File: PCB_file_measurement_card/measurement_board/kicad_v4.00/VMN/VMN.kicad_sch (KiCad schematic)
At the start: 43 parts, among them J1 A/B, J2 Screw_Terminal_VMN, J3 Alim DPH5005, J4 Raspberry_Pi_2_3, K1 AQY211EH, K2 AQY211EH, K3 AQY211EH, K4 AQY211EH, U1 INA128, U2 MCP23008-xP, U3 LM358, U4 INA282, U5 1085-Adress=0X49, U6 1085-Adress=0X48, U7 ISO1540

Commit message: Adds a first version of the PCB to be checked...
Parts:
- R6: footprint Resistor_THT:R_Axial_DIN0411_L9.9mm_D3.6mm_P15.24mm_Horizontal -> Resistor_THT:R_Axial_DIN0414_L11.9mm_D4.5mm_P20.32mm_Horizontal
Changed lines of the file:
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@@
       (effects (font (size 1.27 1.27)) (justify left))
     )
-    (property "Footprint" "Resistor_THT:R_Axial_DIN0411_L9.9mm_D3.6mm_P15.24mm_Horizontal" (id 2) (at 107.442 133.35 90)
+    (property "Footprint" "Resistor_THT:R_Axial_DIN0414_L11.9mm_D4.5mm_P20.32mm_Horizontal" (id 2) (at 107.442 133.35 90)
       (effects (font (size 1.27 1.27)) hide)
     )
@@
   (symbol (lib_id "Device:R") (at 86.36 80.01 0) (unit 1)
     (in_bom yes) (on_board yes)
-    (property "Reference" "R3" (id 0) (at 85.09 80.01 0)
-      (effects (font (size 0.75 0.75)) (justify left))
-    )
-    (property "Value" "1k" (id 1) (at 90.17 82.5499 0)
+    (property "Reference" "R3" (id 0) (at 83.82 78.74 90)
+      (effects (font (size 1.27 1.27)) (justify left))
+    )
+    (property "Value" "1k" (id 1) (at 86.36 81.28 90)
       (effects (font (size 1.27 1.27)) (justify left))
     )
@@
     )
     (path "/4aa539a9-6f3d-4fc3-b2d6-8348016bf7c3"
-      (reference "R6") (unit 1) (value "2") (footprint "Resistor_THT:R_Axial_DIN0411_L9.9mm_D3.6mm_P15.24mm_Horizontal")
+      (reference "R6") (unit 1) (value "2") (footprint "Resistor_THT:R_Axial_DIN0414_L11.9mm_D4.5mm_P20.32mm_Horizontal")
     )
     (path "/cd253d18-2c33-4027-8d8b-dc6d99e23181"

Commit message: update pcb board
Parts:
- added J6: Conn_02x03_Top_Bottom, symbol Connector_Generic:Conn_02x03_Top_Bottom
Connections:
- no-connect marks 56 -> 62
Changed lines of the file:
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@@
   (no_connect (at 153.67 72.39))
   (no_connect (at 153.67 77.47))
+  (no_connect (at 201.93 107.95))
+  (no_connect (at 201.93 110.49))
+  (no_connect (at 201.93 113.03))
+  (no_connect (at 189.23 113.03))
+  (no_connect (at 189.23 110.49))
+  (no_connect (at 189.23 107.95))
   (no_connect (at 252.73 35.56))
   (no_connect (at 255.27 35.56))
@@
     )
     (pin "1")
+  )
+  (symbol (lib_id "Connector_Generic:Conn_02x03_Top_Bottom") (at 194.31 110.49 0) (unit 1)
+    (in_bom yes) (on_board yes) (fields_autoplaced)
+    (property "Reference" "J6" (id 0) (at 195.58 101.6 0))
+    (property "Value" "Conn_02x03_Top_Bottom" (id 1) (at 195.58 104.14 0))
+    (property "Footprint" "" (id 2) (at 194.31 110.49 0)
+      (effects (font (size 1.27 1.27)) hide)
+    )
+    (property "Datasheet" "~" (id 3) (at 194.31 110.49 0)
+      (effects (font (size 1.27 1.27)) hide)
+    )
+    (pin "1")
+    (pin "2")
+    (pin "3")
+    (pin "4")
+    (pin "5")
+    (pin "6")
   )
   (symbol (lib_id "Device:R") (at 109.22 133.35 0) (unit 1)
@@
       (reference "J5") (unit 1) (value "Screw_Terminal_01x02") (footprint "TerminalBlock_Phoenix:TerminalBlock_Phoenix_MKDS-1,5-2-5.08_1x02_P5.08mm_Horizontal")
     )
+    (path "/49058ded-2ed2-473c-ba90-e52b2c428f78"
+      (reference "J6") (unit 1) (value "Conn_02x03_Top_Bottom") (footprint "Connector_IDC:IDC-Header_2x03_P2.54mm_Vertical")
+    )
     (path "/e76f0b41-8ed2-4982-8e0f-a0a6400944d9"

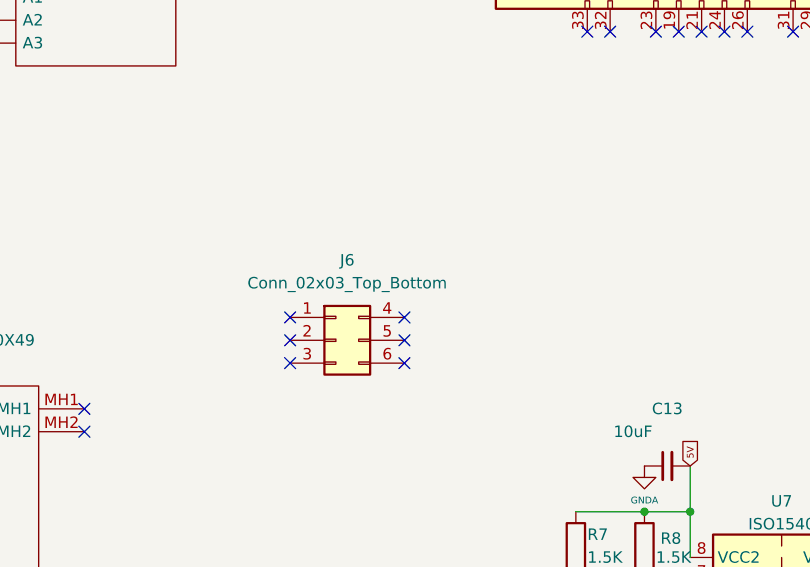
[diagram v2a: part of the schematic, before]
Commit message: update pcb board: +6 pin
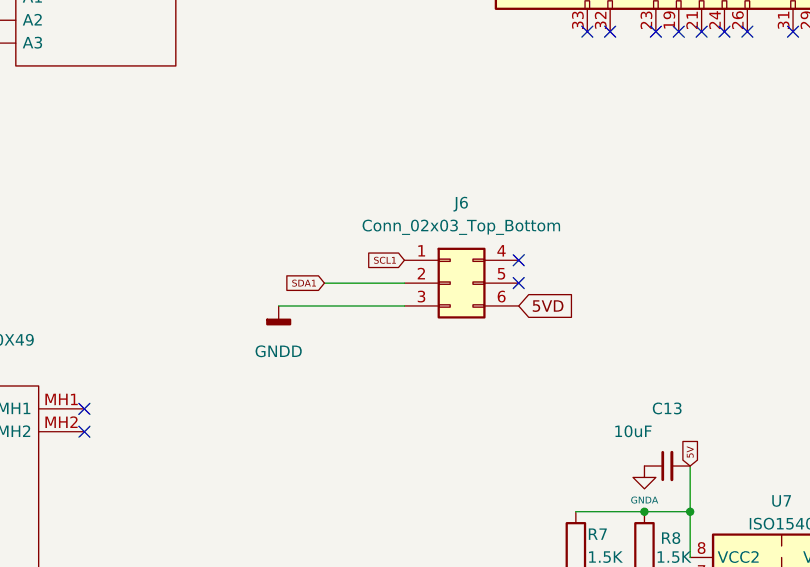
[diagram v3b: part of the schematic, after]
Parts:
- J6: footprint (none) -> Connector_IDC:IDC-Header_2x03_P2.54mm_Vertical
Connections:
- net 5VD: now also J6.6 (Pin_6)
- net GNDD: now also J6.3 (Pin_3)
- net SCL1: now also J6.1 (Pin_1)
- net SDA1: now also J6.2 (Pin_2)
- no-connect marks 62 -> 58
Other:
- moved on the sheet: J6
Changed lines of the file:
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@@
   (no_connect (at 153.67 72.39))
   (no_connect (at 153.67 77.47))
-  (no_connect (at 201.93 107.95))
-  (no_connect (at 201.93 110.49))
-  (no_connect (at 201.93 113.03))
-  (no_connect (at 189.23 113.03))
-  (no_connect (at 189.23 110.49))
-  (no_connect (at 189.23 107.95))
+  (no_connect (at 214.63 101.6))
+  (no_connect (at 214.63 104.14))
   (no_connect (at 252.73 35.56))
   (no_connect (at 255.27 35.56))
@@
     (stroke (width 0) (type default) (color 0 0 0 0))
   )
+  (wire (pts (xy 193.04 104.14) (xy 201.93 104.14))
+    (stroke (width 0) (type default) (color 0 0 0 0))
+  )
   (wire (pts (xy 254 142.24) (xy 257.81 142.24))
     (stroke (width 0) (type default) (color 0 0 0 0))
@@
   )
   (wire (pts (xy 128.27 64.77) (xy 107.95 64.77))
+    (stroke (width 0) (type default) (color 0 0 0 0))
+  )
+  (wire (pts (xy 187.96 106.68) (xy 201.93 106.68))
     (stroke (width 0) (type default) (color 0 0 0 0))
   )
@@
     )
   )
+  (global_label "5VD" (shape input) (at 214.63 106.68 0) (fields_autoplaced)
+    (effects (font (size 1.27 1.27)) (justify left))
+    (property "Intersheet References" "${INTERSHEET_REFS}" (id 0) (at 220.6112 106.6006 0)
+      (effects (font (size 1.27 1.27)) (justify left) hide)
+    )
+  )
   (global_label "B" (shape input) (at 25.4 165.1 90) (fields_autoplaced)
     (effects (font (size 0.75 0.75)) (justify left))
@@
     )
   )
+  (global_label "SCL1" (shape input) (at 201.93 101.6 180) (fields_autoplaced)
+    (effects (font (size 0.75 0.75)) (justify right))
+    (property "Intersheet References" "${INTERSHEET_REFS}" (id 0) (at 197.7192 101.5531 0)
+      (effects (font (size 0.75 0.75)) (justify right) hide)
+    )
+  )
   (global_label "SCL2" (shape input) (at 153.67 59.69 180) (fields_autoplaced)
     (effects (font (size 0.75 0.75)) (justify right))
@@
     (property "Intersheet References" "${INTERSHEET_REFS}" (id 0) (at 277.2608 139.6531 0)
       (effects (font (size 0.75 0.75)) (justify left) hide)
+    )
+  )
+  (global_label "SDA1" (shape input) (at 193.04 104.14 180) (fields_autoplaced)
+    (effects (font (size 0.75 0.75)) (justify right))
+    (property "Intersheet References" "${INTERSHEET_REFS}" (id 0) (at 188.7935 104.0931 0)
+      (effects (font (size 0.75 0.75)) (justify right) hide)
     )
   )
@@
     (pin "2")
   )
+  (symbol (lib_id "power:GNDD") (at 187.96 106.68 0) (unit 1)
+    (in_bom yes) (on_board yes) (fields_autoplaced)
+    (property "Reference" "#PWR?" (id 0) (at 187.96 113.03 0)
+      (effects (font (size 1.27 1.27)) hide)
+    )
+    (property "Value" "GNDD" (id 1) (at 187.96 111.76 0))
+    (property "Footprint" "" (id 2) (at 187.96 106.68 0)
+      (effects (font (size 1.27 1.27)) hide)
+    )
+    (property "Datasheet" "" (id 3) (at 187.96 106.68 0)
+      (effects (font (size 1.27 1.27)) hide)
+    )
+    (pin "1")
+  )
   (symbol (lib_id "Device:C_Small") (at 78.74 63.5 0) (unit 1)
     (in_bom yes) (on_board yes) (fields_autoplaced)
@@
     (pin "1")
   )
-  (symbol (lib_id "Connector_Generic:Conn_02x03_Top_Bottom") (at 194.31 110.49 0) (unit 1)
+  (symbol (lib_id "Connector_Generic:Conn_02x03_Top_Bottom") (at 207.01 104.14 0) (unit 1)
     (in_bom yes) (on_board yes) (fields_autoplaced)
-    (property "Reference" "J6" (id 0) (at 195.58 101.6 0))
-    (property "Value" "Conn_02x03_Top_Bottom" (id 1) (at 195.58 104.14 0))
-    (property "Footprint" "" (id 2) (at 194.31 110.49 0)
-      (effects (font (size 1.27 1.27)) hide)
-    )
-    (property "Datasheet" "~" (id 3) (at 194.31 110.49 0)
+    (property "Reference" "J6" (id 0) (at 208.28 95.25 0))
+    (property "Value" "Conn_02x03_Top_Bottom" (id 1) (at 208.28 97.79 0))
+    (property "Footprint" "Connector_IDC:IDC-Header_2x03_P2.54mm_Vertical" (id 2) (at 207.01 104.14 0)
+      (effects (font (size 1.27 1.27)) hide)
+    )
+    (property "Datasheet" "~" (id 3) (at 207.01 104.14 0)
       (effects (font (size 1.27 1.27)) hide)
     )
@@
       (reference "#PWR039") (unit 1) (value "GNDD") (footprint "")
     )
+    (path "/30873cce-19bb-48ff-a618-d1b628c8f68a"
+      (reference "#PWR?") (unit 1) (value "GNDD") (footprint "")
+    )
     (path "/9f60bb1d-ca92-41d5-b592-f34396aa7479/e59d3cfa-2d20-458f-8209-a7dc300d5c82"

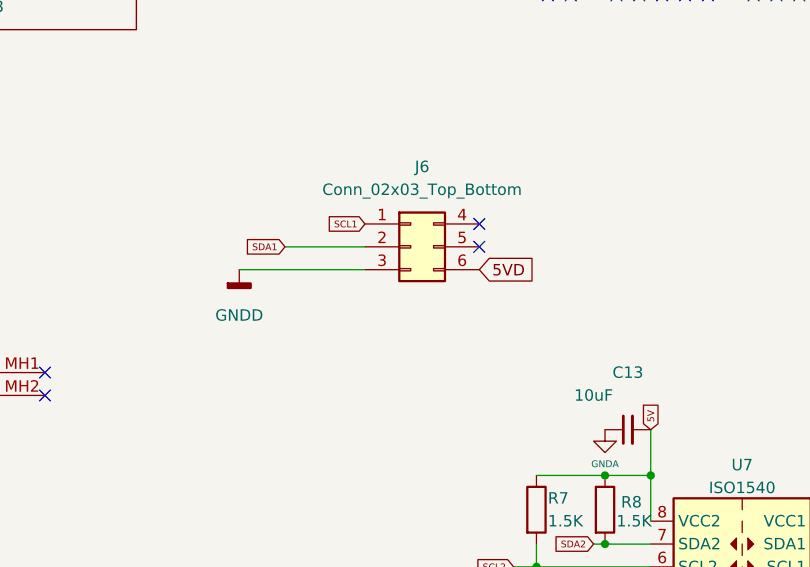
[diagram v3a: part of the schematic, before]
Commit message: Improvements of measurement card v4.00 - change resistors to smaller footprint, adds MUX connector, adds mounting holes
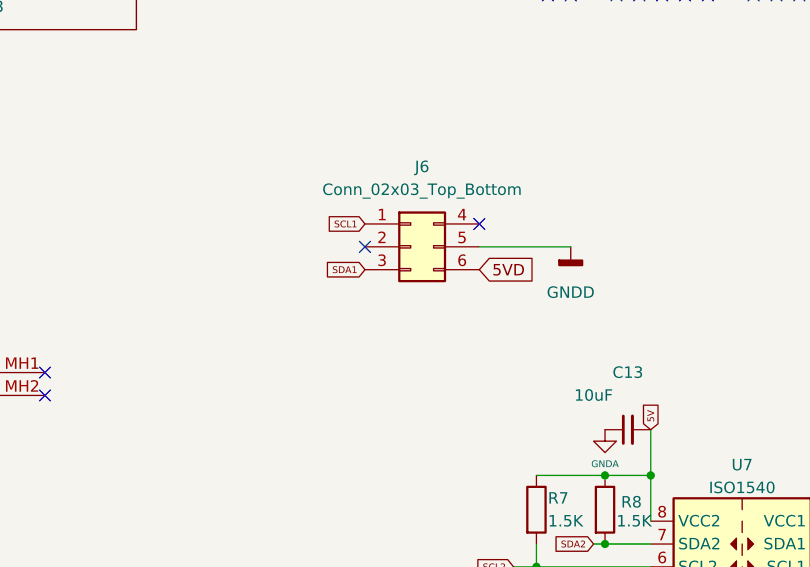
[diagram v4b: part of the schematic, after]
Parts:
- R1, R10, R2, R3, R4, R5, R7, R8, R9: footprint Resistor_THT:R_Axial_DIN0411_L9.9mm_D3.6mm_P15.24mm_Horizontal -> Resistor_THT:R_Axial_DIN0207_L6.3mm_D2.5mm_P7.62mm_Horizontal
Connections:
- net GNDD: now also J6.5 (Pin_5); no longer J6.3 (Pin_3)
- net SDA1: now also J6.3 (Pin_3); no longer J6.2 (Pin_2)
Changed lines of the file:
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@@
   (no_connect (at 153.67 77.47))
   (no_connect (at 214.63 101.6))
-  (no_connect (at 214.63 104.14))
+  (no_connect (at 201.93 104.14))
   (no_connect (at 252.73 35.56))
   (no_connect (at 255.27 35.56))
@@
     (stroke (width 0) (type default) (color 0 0 0 0))
   )
-  (wire (pts (xy 193.04 104.14) (xy 201.93 104.14))
-    (stroke (width 0) (type default) (color 0 0 0 0))
-  )
   (wire (pts (xy 254 142.24) (xy 257.81 142.24))
     (stroke (width 0) (type default) (color 0 0 0 0))
@@
     (stroke (width 0) (type default) (color 0 0 0 0))
   )
+  (wire (pts (xy 214.63 104.14) (xy 224.79 104.14))
+    (stroke (width 0) (type default) (color 0 0 0 0))
+  )
   (wire (pts (xy 109.22 121.92) (xy 109.22 129.54))
     (stroke (width 0) (type default) (color 0 0 0 0))
@@
   )
   (wire (pts (xy 128.27 64.77) (xy 107.95 64.77))
-    (stroke (width 0) (type default) (color 0 0 0 0))
-  )
-  (wire (pts (xy 187.96 106.68) (xy 201.93 106.68))
     (stroke (width 0) (type default) (color 0 0 0 0))
   )
@@
     )
   )
-  (global_label "SDA1" (shape input) (at 193.04 104.14 180) (fields_autoplaced)
+  (global_label "SDA1" (shape input) (at 201.93 106.68 180) (fields_autoplaced)
     (effects (font (size 0.75 0.75)) (justify right))
-    (property "Intersheet References" "${INTERSHEET_REFS}" (id 0) (at 188.7935 104.0931 0)
+    (property "Intersheet References" "${INTERSHEET_REFS}" (id 0) (at 197.6835 106.6331 0)
       (effects (font (size 0.75 0.75)) (justify right) hide)
     )
@@
     (property "Reference" "R4" (id 0) (at 104.14 74.93 90))
     (property "Value" "1k" (id 1) (at 99.06 76.2 90))
-    (property "Footprint" "Resistor_THT:R_Axial_DIN0411_L9.9mm_D3.6mm_P15.24mm_Horizontal" (id 2) (at 99.06 77.978 90)
+    (property "Footprint" "Resistor_THT:R_Axial_DIN0207_L6.3mm_D2.5mm_P7.62mm_Horizontal" (id 2) (at 99.06 77.978 90)
       (effects (font (size 1.27 1.27)) hide)
     )
@@
       (effects (font (size 1.27 1.27)) (justify left))
     )
-    (property "Footprint" "Resistor_THT:R_Axial_DIN0411_L9.9mm_D3.6mm_P15.24mm_Horizontal" (id 2) (at 226.822 133.35 90)
+    (property "Footprint" "Resistor_THT:R_Axial_DIN0207_L6.3mm_D2.5mm_P7.62mm_Horizontal" (id 2) (at 226.822 133.35 90)
       (effects (font (size 1.27 1.27)) hide)
     )
@@
     (pin "2")
   )
-  (symbol (lib_id "power:GNDD") (at 187.96 106.68 0) (unit 1)
+  (symbol (lib_id "power:GNDD") (at 224.79 104.14 0) (unit 1)
     (in_bom yes) (on_board yes) (fields_autoplaced)
-    (property "Reference" "#PWR?" (id 0) (at 187.96 113.03 0)
-      (effects (font (size 1.27 1.27)) hide)
-    )
-    (property "Value" "GNDD" (id 1) (at 187.96 111.76 0))
-    (property "Footprint" "" (id 2) (at 187.96 106.68 0)
-      (effects (font (size 1.27 1.27)) hide)
-    )
-    (property "Datasheet" "" (id 3) (at 187.96 106.68 0)
+    (property "Reference" "#PWR0101" (id 0) (at 224.79 110.49 0)
+      (effects (font (size 1.27 1.27)) hide)
+    )
+    (property "Value" "GNDD" (id 1) (at 224.79 109.22 0))
+    (property "Footprint" "" (id 2) (at 224.79 104.14 0)
+      (effects (font (size 1.27 1.27)) hide)
+    )
+    (property "Datasheet" "" (id 3) (at 224.79 104.14 0)
       (effects (font (size 1.27 1.27)) hide)
     )
@@
       (effects (font (size 1.27 1.27)) (justify left))
     )
-    (property "Footprint" "Resistor_THT:R_Axial_DIN0411_L9.9mm_D3.6mm_P15.24mm_Horizontal" (id 2) (at 258.572 133.35 90)
+    (property "Footprint" "Resistor_THT:R_Axial_DIN0207_L6.3mm_D2.5mm_P7.62mm_Horizontal" (id 2) (at 258.572 133.35 90)
       (effects (font (size 1.27 1.27)) hide)
     )
@@
       (effects (font (size 1.27 1.27)) (justify left))
     )
-    (property "Footprint" "Resistor_THT:R_Axial_DIN0411_L9.9mm_D3.6mm_P15.24mm_Horizontal" (id 2) (at 84.582 80.01 90)
+    (property "Footprint" "Resistor_THT:R_Axial_DIN0207_L6.3mm_D2.5mm_P7.62mm_Horizontal" (id 2) (at 84.582 80.01 90)
       (effects (font (size 1.27 1.27)) hide)
     )
@@
       (effects (font (size 1.27 1.27)) (justify right))
     )
-    (property "Footprint" "Resistor_THT:R_Axial_DIN0411_L9.9mm_D3.6mm_P15.24mm_Horizontal" (id 2) (at 271.018 133.35 90)
+    (property "Footprint" "Resistor_THT:R_Axial_DIN0207_L6.3mm_D2.5mm_P7.62mm_Horizontal" (id 2) (at 271.018 133.35 90)
       (effects (font (size 1.27 1.27)) hide)
     )
@@
       (effects (font (size 1.27 1.27)) (justify left))
     )
-    (property "Footprint" "Resistor_THT:R_Axial_DIN0411_L9.9mm_D3.6mm_P15.24mm_Horizontal" (id 2) (at 35.052 148.59 90)
+    (property "Footprint" "Resistor_THT:R_Axial_DIN0207_L6.3mm_D2.5mm_P7.62mm_Horizontal" (id 2) (at 35.052 148.59 90)
       (effects (font (size 1.27 1.27)) hide)
     )
@@
     (property "Reference" "R5" (id 0) (at 104.14 78.74 90))
     (property "Value" "1k" (id 1) (at 99.06 80.01 90))
-    (property "Footprint" "Resistor_THT:R_Axial_DIN0411_L9.9mm_D3.6mm_P15.24mm_Horizontal" (id 2) (at 99.06 81.788 90)
+    (property "Footprint" "Resistor_THT:R_Axial_DIN0207_L6.3mm_D2.5mm_P7.62mm_Horizontal" (id 2) (at 99.06 81.788 90)
       (effects (font (size 1.27 1.27)) hide)
     )
@@
       (effects (font (size 1.27 1.27)) (justify left))
     )
-    (property "Footprint" "Resistor_THT:R_Axial_DIN0411_L9.9mm_D3.6mm_P15.24mm_Horizontal" (id 2) (at 219.202 133.35 90)
+    (property "Footprint" "Resistor_THT:R_Axial_DIN0207_L6.3mm_D2.5mm_P7.62mm_Horizontal" (id 2) (at 219.202 133.35 90)
       (effects (font (size 1.27 1.27)) hide)
     )
@@
       (effects (font (size 1.27 1.27)) (justify left))
     )
-    (property "Footprint" "Resistor_THT:R_Axial_DIN0411_L9.9mm_D3.6mm_P15.24mm_Horizontal" (id 2) (at 69.342 148.59 90)
+    (property "Footprint" "Resistor_THT:R_Axial_DIN0207_L6.3mm_D2.5mm_P7.62mm_Horizontal" (id 2) (at 69.342 148.59 90)
       (effects (font (size 1.27 1.27)) hide)
     )
@@
     )
     (path "/30873cce-19bb-48ff-a618-d1b628c8f68a"
-      (reference "#PWR?") (unit 1) (value "GNDD") (footprint "")
+      (reference "#PWR0101") (unit 1) (value "GNDD") (footprint "")
     )
     (path "/9f60bb1d-ca92-41d5-b592-f34396aa7479/e59d3cfa-2d20-458f-8209-a7dc300d5c82"
@@
     )
     (path "/78d1bcfe-6a0d-43b3-b124-bba408aabe9a"
-      (reference "R1") (unit 1) (value "1.5k") (footprint "Resistor_THT:R_Axial_DIN0411_L9.9mm_D3.6mm_P15.24mm_Horizontal")
+      (reference "R1") (unit 1) (value "1.5k") (footprint "Resistor_THT:R_Axial_DIN0207_L6.3mm_D2.5mm_P7.62mm_Horizontal")
     )
     (path "/cd369a1d-d2ff-4295-a91a-5d9f602bcafc"
-      (reference "R2") (unit 1) (value "1.5k") (footprint "Resistor_THT:R_Axial_DIN0411_L9.9mm_D3.6mm_P15.24mm_Horizontal")
+      (reference "R2") (unit 1) (value "1.5k") (footprint "Resistor_THT:R_Axial_DIN0207_L6.3mm_D2.5mm_P7.62mm_Horizontal")
     )
     (path "/4ee9ddd6-851b-4b78-9262-c1f951cd0ce2"
-      (reference "R3") (unit 1) (value "1k") (footprint "Resistor_THT:R_Axial_DIN0411_L9.9mm_D3.6mm_P15.24mm_Horizontal")
+      (reference "R3") (unit 1) (value "1k") (footprint "Resistor_THT:R_Axial_DIN0207_L6.3mm_D2.5mm_P7.62mm_Horizontal")
     )
     (path "/160d7993-0220-4204-85b6-881694d41594"
-      (reference "R4") (unit 1) (value "1k") (footprint "Resistor_THT:R_Axial_DIN0411_L9.9mm_D3.6mm_P15.24mm_Horizontal")
+      (reference "R4") (unit 1) (value "1k") (footprint "Resistor_THT:R_Axial_DIN0207_L6.3mm_D2.5mm_P7.62mm_Horizontal")
     )
     (path "/9da9e877-ee2d-4701-9fc4-2fe9a669f811"
-      (reference "R5") (unit 1) (value "1k") (footprint "Resistor_THT:R_Axial_DIN0411_L9.9mm_D3.6mm_P15.24mm_Horizontal")
+      (reference "R5") (unit 1) (value "1k") (footprint "Resistor_THT:R_Axial_DIN0207_L6.3mm_D2.5mm_P7.62mm_Horizontal")
     )
     (path "/4aa539a9-6f3d-4fc3-b2d6-8348016bf7c3"
@@
     )
     (path "/cd253d18-2c33-4027-8d8b-dc6d99e23181"
-      (reference "R7") (unit 1) (value "1.5K") (footprint "Resistor_THT:R_Axial_DIN0411_L9.9mm_D3.6mm_P15.24mm_Horizontal")
+      (reference "R7") (unit 1) (value "1.5K") (footprint "Resistor_THT:R_Axial_DIN0207_L6.3mm_D2.5mm_P7.62mm_Horizontal")
     )
     (path "/2d52f746-0700-47cd-baa9-f865098d36e4"
-      (reference "R8") (unit 1) (value "1.5K") (footprint "Resistor_THT:R_Axial_DIN0411_L9.9mm_D3.6mm_P15.24mm_Horizontal")
+      (reference "R8") (unit 1) (value "1.5K") (footprint "Resistor_THT:R_Axial_DIN0207_L6.3mm_D2.5mm_P7.62mm_Horizontal")
     )
     (path "/31817ade-7cdb-4a1c-b1b9-415ea1cb12e4"
-      (reference "R9") (unit 1) (value "1.5k") (footprint "Resistor_THT:R_Axial_DIN0411_L9.9mm_D3.6mm_P15.24mm_Horizontal")
+      (reference "R9") (unit 1) (value "1.5k") (footprint "Resistor_THT:R_Axial_DIN0207_L6.3mm_D2.5mm_P7.62mm_Horizontal")
     )
     (path "/659bf650-0875-49cb-82d5-50a4a9df21b5"
-      (reference "R10") (unit 1) (value "1.5k") (footprint "Resistor_THT:R_Axial_DIN0411_L9.9mm_D3.6mm_P15.24mm_Horizontal")
+      (reference "R10") (unit 1) (value "1.5k") (footprint "Resistor_THT:R_Axial_DIN0207_L6.3mm_D2.5mm_P7.62mm_Horizontal")
     )
     (path "/3bf56d6f-48a1-4578-b98f-cb42bf57daee"
